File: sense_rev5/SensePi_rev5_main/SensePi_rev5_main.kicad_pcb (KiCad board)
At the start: 2 copper layers, 60 x 38 mm, 55 parts, among them J1 PJ-611-5A_AudioJack, J2 Conn_01x02, J3 Conn_01x06, Q1 TSM2301, Q2 Q_DUAL_NMOS_BSD840NH6327XTSA1, Q4 Q_Photo_NPN, SW1 SW_SPST, SW2 Slider_Switch_SW_2_State, U1 MDBT42Q, U2 MCP4012T-503E/CH, U3 TLV8802, U4 PIR, Y1 Crystal

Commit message: sense_rev5 PCB Design files completed.
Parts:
- moved J3 4.03 mm to (46.5, 47.0)
- moved MK2 4.03 mm to (64.5, 48.0)
- moved R12 3.79 mm to (47.0, 43.5), turned to 270 degrees
- moved C13 3.63 mm to (48.2, 43.5), turned to 270 degrees
- moved C1 3.50 mm to (59.6, 20.0)
- moved C3 3.50 mm to (54.8, 20.0)
- moved C4 3.50 mm to (48.9, 23.1)
- moved C5 3.50 mm to (56.0, 20.0)
- moved C6 3.50 mm to (48.9, 25.7)
- moved L1 3.50 mm to (58.4, 20.0)
- moved L2 3.50 mm to (57.2, 20.0)
- moved MK3 3.50 mm to (64.5, 12.0)
- moved U1 3.50 mm to (60.5, 27.5)
- moved Y1 3.50 mm to (51.0, 24.4)
- moved J2 2.00 mm to (51.3, 42.0)
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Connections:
- net /GPIO2 renamed Net-(U1-Pad32)
- J3 pad 5: /SWDIO -> /SWDCLK
- J3 pad 6: /SWDCLK -> /SWDIO
- U1 pad 31: /RX -> Net-(U1-Pad31)
- U1 pad 33: /GPIO1 -> /RX
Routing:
- net VDD: track 0.00 -> 130.7 mm, vias 0 -> 3
- net GND: track 0.00 -> 69.9 mm, vias 0 -> 30
- net /LED_SENSE: track 0.00 -> 60.3 mm, vias 0 -> 4
- net /OUT_A: track 0.00 -> 45.2 mm, vias 0 -> 3
- net /FOCUS: track 0.00 -> 43.3 mm, vias 0 -> 2
- net /AMP_SIGNAL: track 0.00 -> 40.8 mm, vias 0 -> 4
- net /TRIGGER: track 0.00 -> 37.5 mm, vias 0 -> 2
- net /AUDIO_JACK_IO: track 0.00 -> 36.1 mm, vias 0 -> 2
- net /LED_GREEN: track 0.00 -> 34.5 mm, vias 0 -> 2
- net /LED_RED: track 0.00 -> 25.7 mm, vias 0 -> 2
- net /PIR_OUT: track 0.00 -> 24.2 mm
- net /RX: track 0.00 -> 18.8 mm
- net /TX: track 0.00 -> 18.1 mm
- net /SWDCLK: track 0.00 -> 17.6 mm
- net /MCP4012T_U\D: track 0.00 -> 17.6 mm
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- added copper zone on B.Cu, net GND
- added copper zone on F.Cu, net GND
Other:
- board size 60 x 38 mm -> 56.5 x 40 mm

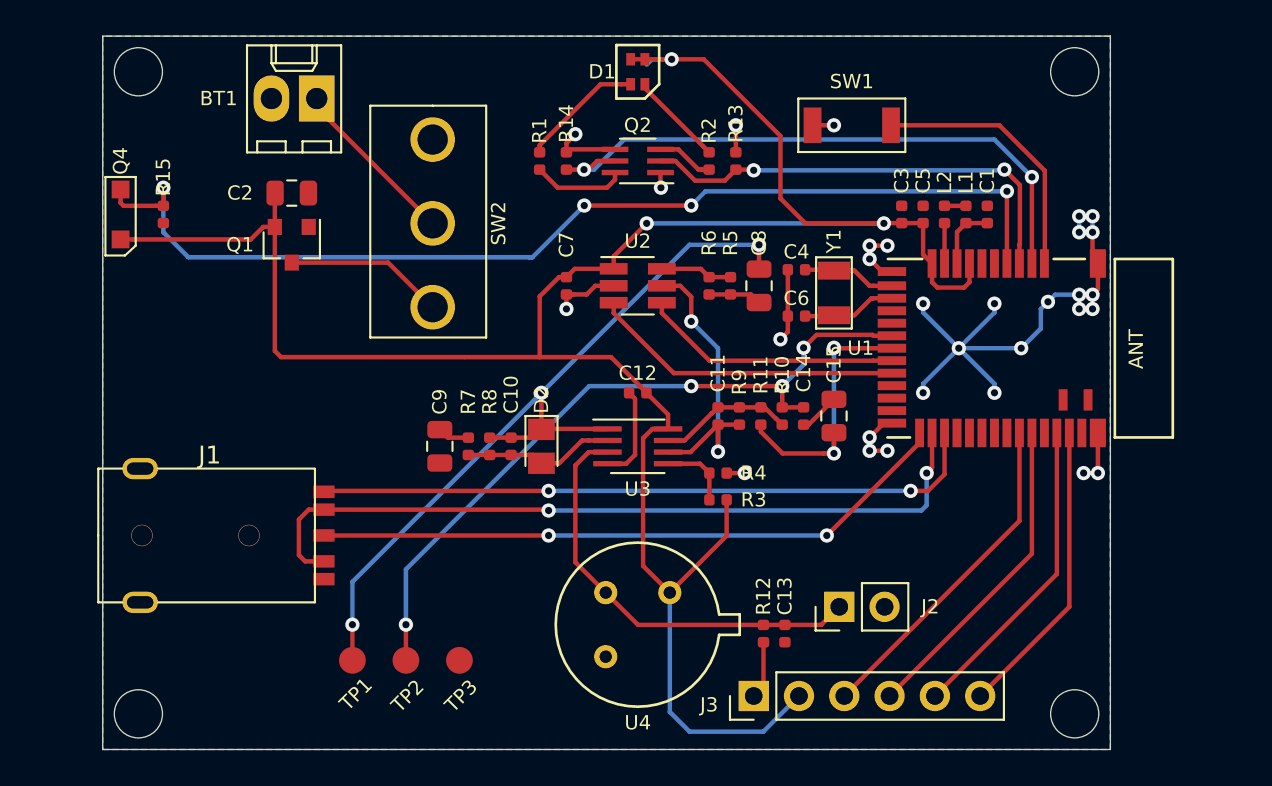
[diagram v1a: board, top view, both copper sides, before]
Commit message: senseBe_rev4 and sense_rev5 schematic and PCB placement done.
PCB placement for all major components that affect the mechanical enclosure design is done, and locked.
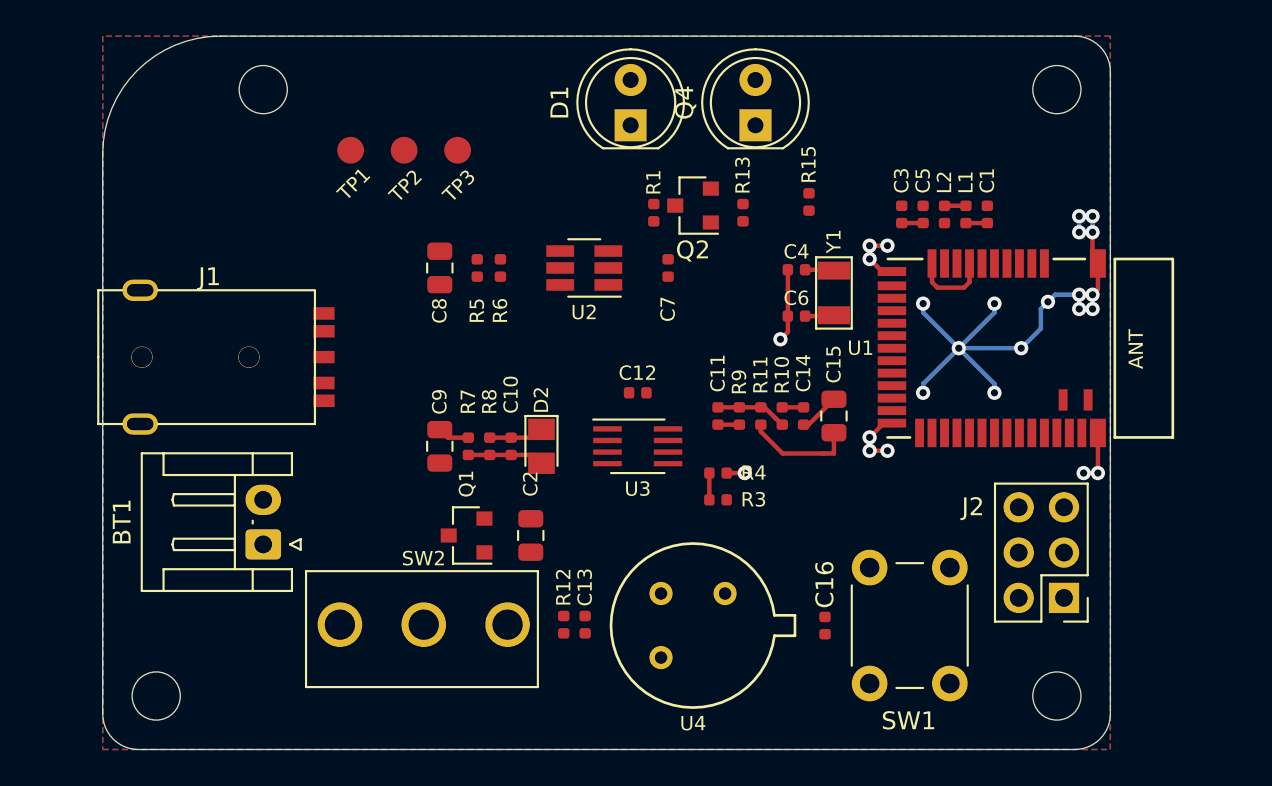
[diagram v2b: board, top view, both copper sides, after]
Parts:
- removed J3: Conn_01x06, Connector_PinHeader_2.54mm:PinHeader_1x06_P2.54mm_Vertical
- removed R14: 470k, Resistor_SMD:R_0402_1005Metric
- removed R2: 33E, Resistor_SMD:R_0402_1005Metric
- added C16: 100nF, Capacitor_SMD:C_0402_1005Metric, F.Cu at (50.5, 43.0)
- BT1: footprint sense:Molex_KK-6410-02_02x2.54mm_Straight -> Connector_JST:JST_EH_S2B-EH_1x02_P2.50mm_Horizontal
- D1: value LED_Dual_ACAC -> LED; footprint sense:18-225_R6G6C-A01_3T -> LED_THT:LED_D5.0mm
- J2: value Conn_01x02 -> Conn_02x03_Odd_Even; footprint Connector_PinHeader_2.54mm:PinHeader_1x02_P2.54mm_Vertical -> Connector_PinHeader_2.54mm:PinHeader_2x03_P2.54mm_Vertical
- Q2: value Q_DUAL_NMOS_BSD840NH6327XTSA1 -> 2N7002; footprint sense:BSD840NH6327XTSA1_Dual_NMOS -> sense:SOT-23
- Q4: footprint sense:PT12-21C TR8PhotoTransistor -> LED_THT:LED_D5.0mm
- SW1: footprint sense:TACTILE SWITCH 3X4X2MM SMD 2-PIN -> sense:SW_PUSH_6mm
- moved R15 36.2 mm to (49.6, 19.3)
- moved Q4 35.9 mm to (46.6, 15.0)
- moved TP1 28.6 mm to (23.9, 16.4)
- moved TP2 28.6 mm to (26.9, 16.4)
- moved TP3 28.6 mm to (29.9, 16.4)
- moved SW1 25.4 mm to (57.5, 39.8), turned to 270 degrees
- moved BT1 25.2 mm to (19.0, 38.5), turned to 90 degrees
- moved C2 23.4 mm to (34.0, 38.0), turned to 270 degrees
- moved SW2 22.5 mm to (28.0, 43.0), turned to 0 degrees
- moved Q1 19.0 mm to (30.4, 38.0), turned to 180 degrees
- moved C8 17.9 mm to (28.9, 23.0), turned to 270 degrees
- moved R5 14.2 mm to (31.0, 23.0), turned to 90 degrees
- moved J2 12.6 mm to (63.9, 41.5), turned to 180 degrees
- moved R6 11.7 mm to (32.3, 23.0), turned to 90 degrees
- moved C13 11.2 mm to (37.0, 43.0)
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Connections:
- D1 pad 1: VDD -> Net-(D1-Pad1)
- D1 pad 2: Net-(D1-Pad2) -> VDD
- J2 pad 1: /PIR_OUT -> /SWDIO
- J2 pad 2: GND -> /RX
- Q2 pad 1: GND -> /LED_RED
- Q2 pad 2: /LED_RED -> GND
- R1 pad 1: Net-(Q2-Pad6) -> Net-(Q2-Pad3)
- R1 pad 2: Net-(D1-Pad4) -> Net-(D1-Pad1)
- U1 pad 3: /LED_GREEN -> /LED_RED
- U1 pad 4: /LED_RED -> Net-(U1-Pad4)
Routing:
- net VDD: track 130.7 -> 5.65 mm, vias 3 -> 0
- net /LED_SENSE: track 60.3 -> 0.00 mm, vias 4 -> 0
- net /FOCUS: track 43.3 -> 0.00 mm, vias 2 -> 0
- net /OUT_A: track 45.2 -> 3.09 mm, vias 3 -> 0
- net /AMP_SIGNAL: track 40.8 -> 1.20 mm, vias 4 -> 0
- net /TRIGGER: track 37.5 -> 0.00 mm, vias 2 -> 0
- net /AUDIO_JACK_IO: track 36.1 -> 0.00 mm, vias 2 -> 0
- net /LED_GREEN: track 34.5 -> 0.00 mm, vias 2 -> 0
- net /LED_RED: track 25.7 -> 0.00 mm, vias 2 -> 0
- net /PIR_OUT: track 24.2 -> 0.00 mm
- net GND: track 69.9 -> 50.0 mm, vias 30 -> 25
- net /RX: track 18.8 -> 0.00 mm
- net /TX: track 18.1 -> 0.00 mm
- net /SWDCLK: track 17.6 -> 0.00 mm
- net /MCP4012T_U\D: track 17.6 -> 0.00 mm
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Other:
- outline, holes or cut-outs redrawn
- board text added: "www.appiko.org"

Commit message: Rev 5 of SensePi board final
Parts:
- removed Q4: Q_Photo_NPN, LED_THT:LED_D5.0mm
- removed TP1, TP2, TP3: TEST, sense:Measurement_Point_Round-SMD-Pad_Small
- added BT2: CR2032 holder, sense_fp:BatteryHolder_Keystone_3009_1x2450, B.Cu at (30.1, 26.8)
- added C19: 0.1uF, sense_fp:C_0402_1005Metric, F.Cu at (48.0, 38.8)
- added G***: LOGO, sense_fp:OSHW1, B.Cu at (52.8, 28.3)
- added G***: Appiko_LOGO_img, sense_fp:Appiko_LOGO_img, F.Cu at (23.9, 21.8)
- added G***: Appiko_Logo_2, sense_fp:Appiko_Logo_2, F.Cu at (36.2, 20.0)
- added GND: TEST, sense_fp:Measurement_Point_Round-SMD-Pad_Small, F.Cu at (13.9, 18.3)
- added OUT1: TEST, sense_fp:Measurement_Point_Round-SMD-Pad_Small, F.Cu at (34.9, 37.8)
- added OUT2: TEST, sense_fp:Measurement_Point_Round-SMD-Pad_Small, F.Cu at (46.5, 27.0)
- added R2: LDR, sense_fp:LED_D5.0mm, F.Cu at (46.6, 15.0)
- added U5: PCF8563T, sense_fp:SOIC-8_3.9x4.9mm_P1.27mm, F.Cu at (50.2, 35.4)
- added Y2: Q13FC1350000400, sense_fp:Q13FC1350000400_SMD Crystals 32.768KHz, F.Cu at (55.2, 36.1)
- BT1: value Battery -> 2xAA_molex; footprint Connector_JST:JST_EH_S2B-EH_1x02_P2.50mm_Horizontal -> sense_fp:JST_EH_S2B-EH_1x02_P2.50mm_Horizontal
- C1, C3: footprint Capacitor_SMD:C_0402_1005Metric -> sense_fp:C_0603_1608Metric
- C10, C11, C12, C14, C4, C6, C7: footprint Capacitor_SMD:C_0402_1005Metric -> sense_fp:C_0402_1005Metric
- C13, C5: value 100nF -> 0.1uF; footprint Capacitor_SMD:C_0402_1005Metric -> sense_fp:C_0402_1005Metric
- C15, C8, C9: footprint Capacitor_SMD:C_0805_2012Metric -> sense_fp:C_1206_3216Metric
- C16: value 100nF -> 0.1nF; footprint Capacitor_SMD:C_0402_1005Metric -> sense_fp:C_0402_1005Metric
- C2: value 10uF -> 22uF; footprint Capacitor_SMD:C_0805_2012Metric -> sense_fp:C_1206_3216Metric
- D1: value LED -> C503B-RAN-CZ0C0AA1; footprint LED_THT:LED_D5.0mm -> sense_fp:LED_D5.0mm
- D2: footprint Diode_SMD:D_MicroMELF -> sense_fp:D_SOD-323
- J1: footprint sense:PJ_611_5A_Audio Jack -> sense_fp:PJ_611_5A_Audio Jack
- J2: footprint Connector_PinHeader_2.54mm:PinHeader_2x03_P2.54mm_Vertical -> sense_fp:PinHeader_2x03_P2.54mm_Vertical
- L1: value 15nH -> 18nH; footprint Inductor_SMD:L_0402_1005Metric -> sense_fp:C_0603_1608Metric
- L2: value 10nH -> 10uH; footprint Inductor_SMD:L_0402_1005Metric -> sense_fp:L_0805
- MK1, MK2, MK3, MK4: footprint MountingHole:MountingHole_2.7mm_M2.5 -> sense_fp:MountingHole_2.7mm_M2.5
- Q1: value TSM2301 -> IRLML6401; footprint sense:SOT-23 -> sense_fp:SOT-23
- Q2: value 2N7002 -> SI2302; footprint sense:SOT-23 -> sense_fp:SOT-23
- R1, R10, R11, R12, R3, R4, R5, R6, R7, R8, R9: footprint Resistor_SMD:R_0402_1005Metric -> sense_fp:C_0402_1005Metric
- R13: value 470k -> 47k; footprint Resistor_SMD:R_0402_1005Metric -> sense_fp:C_0402_1005Metric
- SW1: footprint sense:SW_PUSH_6mm -> sense_fp:SW_PUSH_6mm
- SW2: footprint sense:SlideSwitch_1P2T_Straight -> sense_fp:SlideSwitch_1P2T_Straight
- U1: footprint sense:mdbt42Q -> sense_fp:mdbt42Q
- U2: footprint sense:SOT-23-6_Handsoldering -> sense_fp:SOT-23-6
- U3: value TLV8802 -> TLV522; footprint sense:SSOP-8_2.95x2.8mm_Pitch0.65mm -> sense_fp:SSOP-8_2.95x2.8mm_Pitch0.65mm
- U4: footprint sense:PIR_TO5 -> sense_fp:PIR_TO5
- Y1: value Crystal -> Q13FC1350000400; footprint sense:Q13FC1350000400_SMD Crystals 32.768KHz -> sense_fp:Q13FC1350000400_SMD Crystals 32.768KHz
- moved Q2 15.4 mm to (57.9, 15.3), turned to 270 degrees
- moved R1 14.6 mm to (55.1, 16.4), turned to 180 degrees
- moved R13 13.9 mm to (57.9, 12.9), turned to 180 degrees
- moved C2 12.8 mm to (35.5, 25.3), turned to 90 degrees
- moved R5 11.3 mm to (40.3, 29.5), turned to 270 degrees
- moved R6 11.2 mm to (41.4, 29.5), turned to 270 degrees
- moved C8 10.5 mm to (37.4, 29.2), turned to 180 degrees
- moved U2 9.77 mm to (44.2, 29.6)
- moved C7 8.77 mm to (46.7, 30.2)
- moved Q1 8.35 mm to (36.4, 43.8)
- moved R7 7.78 mm to (38.2, 34.1), turned to 180 degrees
- moved R8 7.50 mm to (38.7, 35.7), turned to 90 degrees
- moved C13 7.04 mm to (41.8, 37.8), turned to 0 degrees
- moved C9 6.84 mm to (35.7, 32.3), turned to 180 degrees
- moved R15 6.50 mm to (51.2, 13.0)
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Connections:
- net /LED_SENSE renamed /LDR_SENSE
- U1 pad 15: Net-(U1-Pad15) -> /MCP4012T_CS
- U1 pad 16: Net-(U1-Pad16) -> /MCP4012T_U\D
- U1 pad 19: /MCP4012T_CS -> Net-(U1-Pad19)
- U1 pad 2: /BUTTON -> Net-(U1-Pad2)
- U1 pad 20: /MCP4012T_U\D -> Net-(U1-Pad20)
- U1 pad 21: Net-(U1-Pad21) -> /SDA
- U1 pad 22: Net-(U1-Pad22) -> /SCL
- U1 pad 23: Net-(U1-Pad23) -> /RTC_CLK
- U1 pad 25: /AUDIO_JACK_IO -> /RTC_INT
- U1 pad 26: /FOCUS -> /BUTTON
- U1 pad 28: Net-(U1-Pad28) -> /FOCUS
- U1 pad 29: Net-(U1-Pad29) -> /AUDIO_JACK_IO
- U1 pad 3: /LED_RED -> Net-(U1-Pad3)
- U1 pad 4: Net-(U1-Pad4) -> /LED_RED
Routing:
- net VDD: track 5.65 -> 199.9 mm, vias 0 -> 2
- net GND: track 50.0 -> 128.4 mm, vias 25 -> 34
- net /FOCUS: track 0.00 -> 71.9 mm
- net /AUDIO_JACK_IO: track 0.00 -> 66.8 mm
- net /TRIGGER: track 0.00 -> 64.2 mm
- net Net-(BT2-Pad1): track 0.00 -> 51.3 mm
- net /LDR_SENSE: track 0.00 -> 23.7 mm
- net /BUTTON: track 0.00 -> 18.6 mm
- net Net-(D1-Pad1): track 0.00 -> 18.0 mm
- net /MCP4012T_CS: track 0.00 -> 13.1 mm
- net /LED_RED: track 0.00 -> 11.8 mm
- net /MCP4012T_U\D: track 0.00 -> 11.5 mm
- net Net-(BT1-Pad1): track 0.00 -> 10.9 mm
- net /OUT_A: track 3.09 -> 13.7 mm
- net /RX: track 0.00 -> 10.6 mm
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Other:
- net class Default: clearance 0.2 -> 0.15
- rule trace_clearance: 0.2 -> 0.15
- board text added: "SensePi rev5"
- board text added: "appiko.org"
- board text removed: "www.appiko.org"

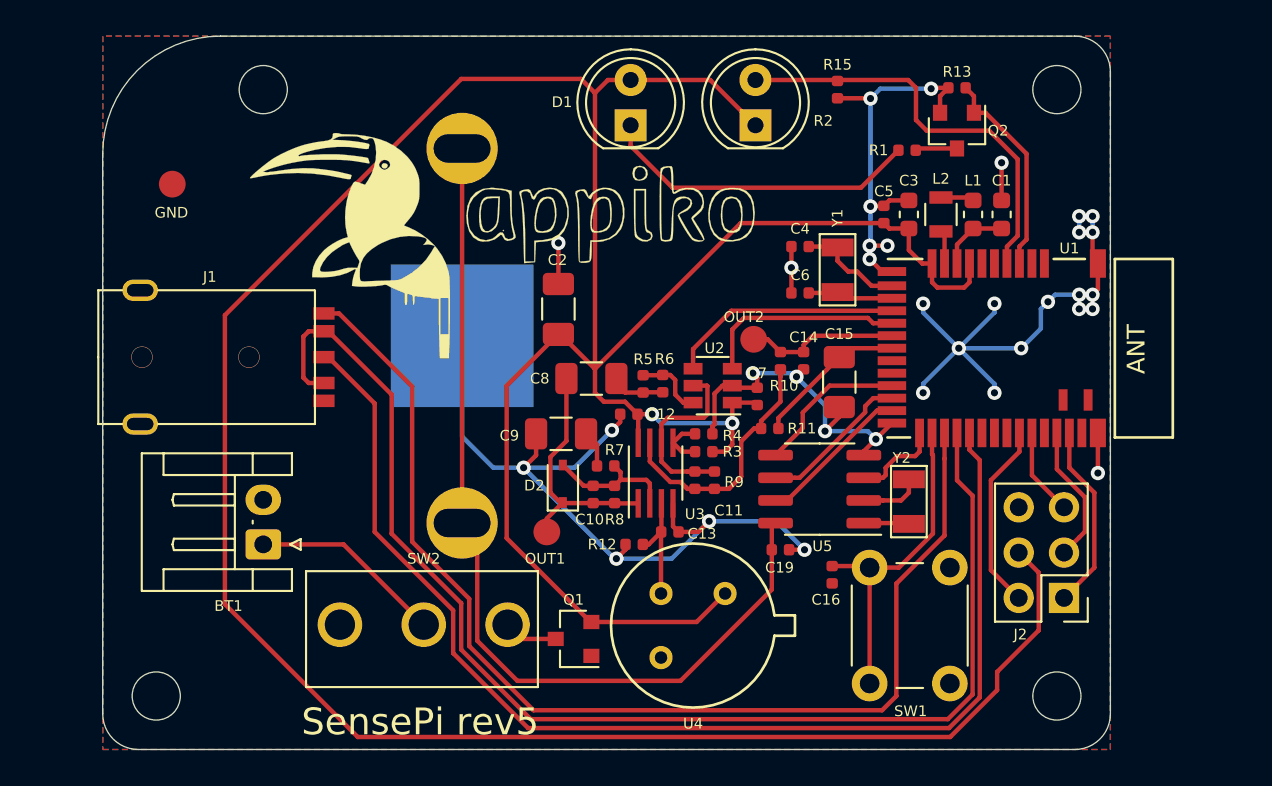
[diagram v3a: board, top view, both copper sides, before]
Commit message: Updated PCB with VDD control of LDR and PIR circuitry
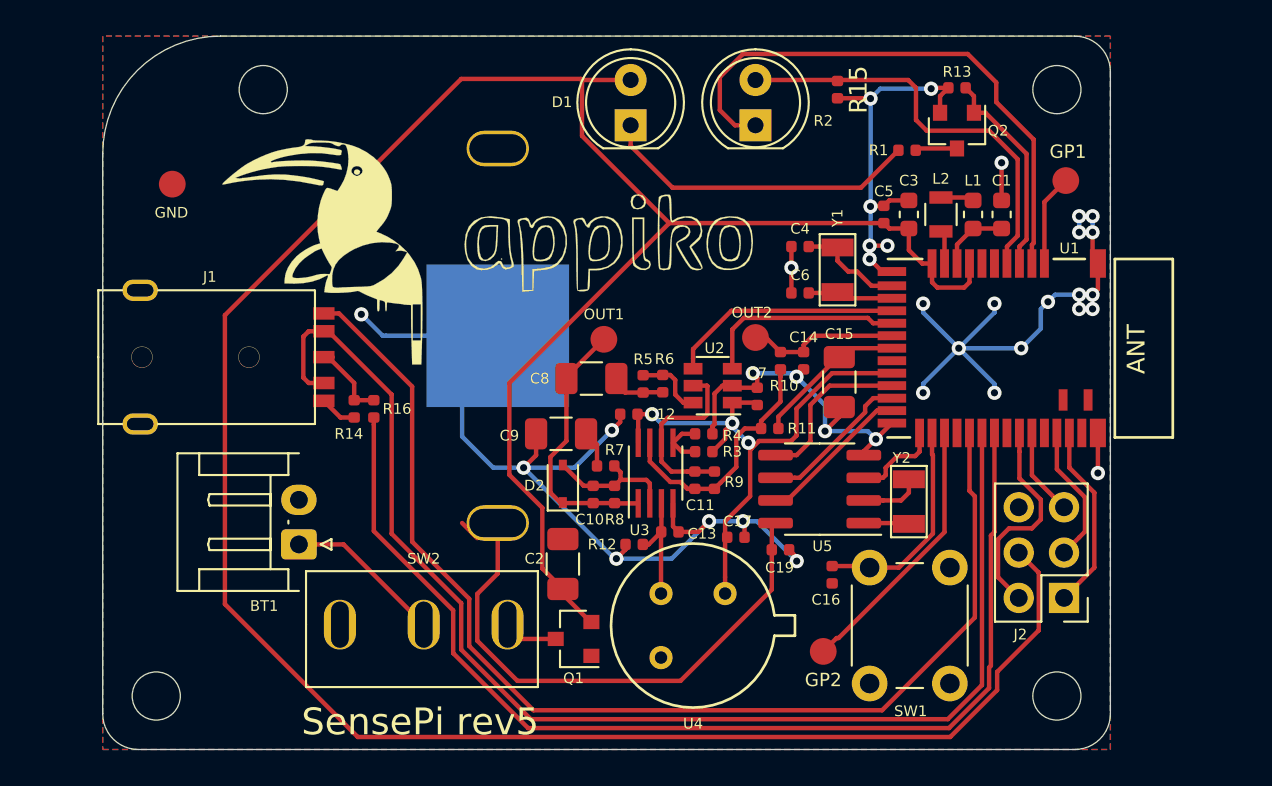
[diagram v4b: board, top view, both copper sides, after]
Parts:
- added C17: 0.1uF, sense_fp:C_0402_1005Metric, F.Cu at (45.5, 38.1)
- added GP1: GP1, sense_fp:Measurement_Point_Round-SMD-Pad_Small, F.Cu at (64.0, 18.1)
- added GP2: GP3, sense_fp:Measurement_Point_Round-SMD-Pad_Small, F.Cu at (50.4, 44.5)
- added R14: 1.2k, sense_fp:C_0402_1005Metric, F.Cu at (24.1, 30.9)
- added R16: 1k, sense_fp:C_0402_1005Metric, F.Cu at (25.2, 30.9)
- GND: value TEST -> GND
- OUT1: value TEST -> OUT1
- OUT2: value TEST -> OUT2
- R15: footprint Resistor_SMD:R_0402_1005Metric -> sense_fp:C_0402_1005Metric
- moved C2 14.3 mm to (35.8, 39.6)
- moved OUT1 11.3 mm to (38.1, 27.0)
- moved G*** 5.90 mm to (56.5, 23.7)
- moved BT1 2.00 mm to (21.0, 38.5)
- moved BT2 2.00 mm to (32.1, 26.8)
- moved G*** 1.60 mm to (36.1, 21.6)
- moved G*** 1.59 mm to (22.3, 22.1)
- moved OUT2 0.14 mm to (46.6, 26.9)
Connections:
- C12 pad 1: VDD -> /VDD_PIR
- C7 pad 1: VDD -> /VDD_PIR
- J1 pad 3: /AUDIO_JACK_IO -> Net-(J1-Pad3)
- R2 pad 1: VDD -> /LDR_SENSE_EN
- R3 pad 1: VDD -> /VDD_PIR
- U1 pad 20: Net-(U1-Pad20) -> /VDD_PIR
- U1 pad 27: /TRIGGER -> Net-(TP6-Pad1)
- U1 pad 28: /FOCUS -> Net-(U1-Pad28)
- U1 pad 29: /AUDIO_JACK_IO -> /TRIGGER
- U1 pad 3: Net-(U1-Pad3) -> /LDR_SENSE_EN
- U1 pad 30: Net-(U1-Pad30) -> /FOCUS
- U1 pad 31: Net-(U1-Pad31) -> /AUDIO_JACK_IO
- U2 pad 1: VDD -> /VDD_PIR
- U3 pad 8: VDD -> /VDD_PIR
- U4 pad 1: VDD -> /VDD_PIR
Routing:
- net VDD: track 199.9 -> 160.0 mm, vias 2 -> 0
- net /VDD_PIR: track 0.00 -> 32.9 mm, vias 0 -> 3
- net /LDR_SENSE_EN: track 0.00 -> 32.0 mm
- net Net-(BT2-Pad1): track 51.3 -> 31.7 mm
- net Net-(TP6-Pad1): track 0.00 -> 15.1 mm
- net GND: track 128.4 -> 135.0 mm, vias 34 -> 35
- net /BUTTON: track 18.6 -> 12.1 mm
- net Net-(TP4-Pad1): track 0.00 -> 5.15 mm
- net Net-(J1-Pad3): track 0.00 -> 4.87 mm
- net /AUDIO_JACK_IO: track 66.8 -> 62.2 mm
- net Net-(BT1-Pad1): track 10.9 -> 8.86 mm
- net /RX: track 10.6 -> 12.0 mm
- net /OUT_A: track 13.7 -> 14.7 mm
- net /TRIGGER: track 64.2 -> 65.0 mm
- net /SDA: track 8.64 -> 9.33 mm
